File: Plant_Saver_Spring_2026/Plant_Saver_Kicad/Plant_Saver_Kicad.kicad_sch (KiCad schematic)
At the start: 21 parts, among them SW1 Up, SW2 Down, SW3 Change Screen, SW4 Select, SW5 Select, U14 CDBA140SL-HF, U18 ESP32-WROOM-32E-N16, U3 ESP32-WROOM-32D, U5 CDBA140SL-HF, U6 CDBA140SL-HF, U7 CDBA140SL-HF

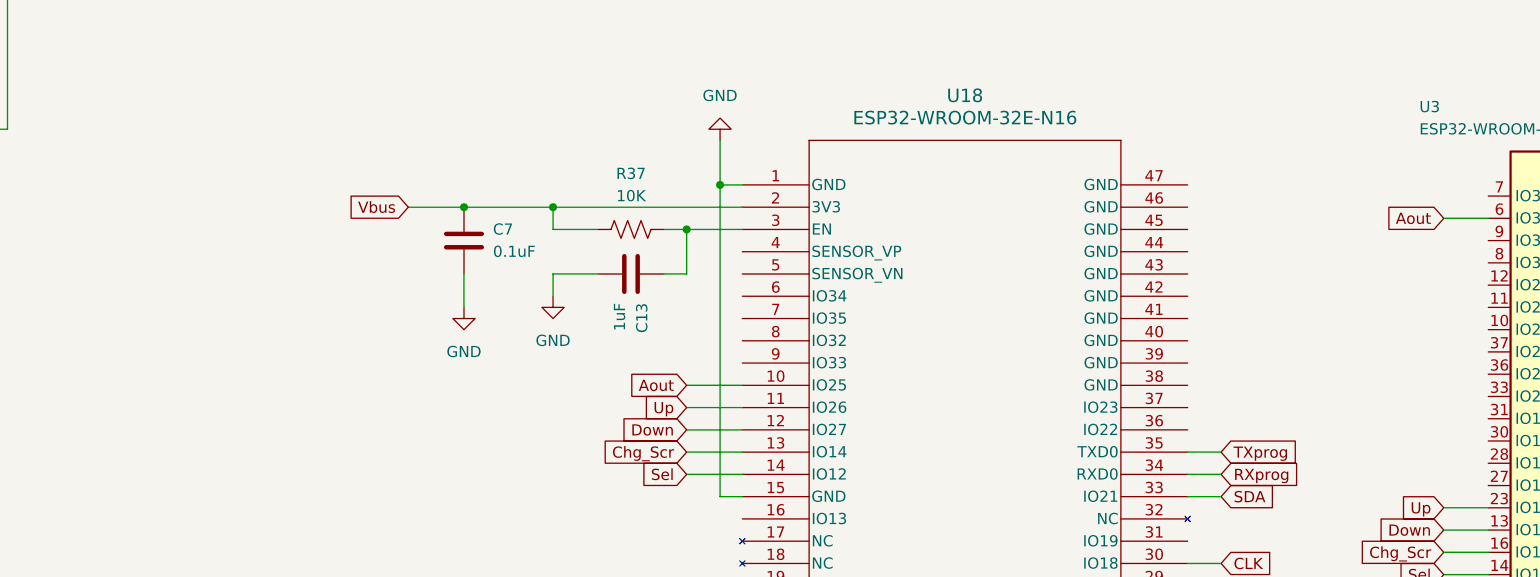
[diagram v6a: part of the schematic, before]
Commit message: Schematic updates
Added USB charge LEDs, updated PMOS gates, added micro connections and revised some of the charging set up.
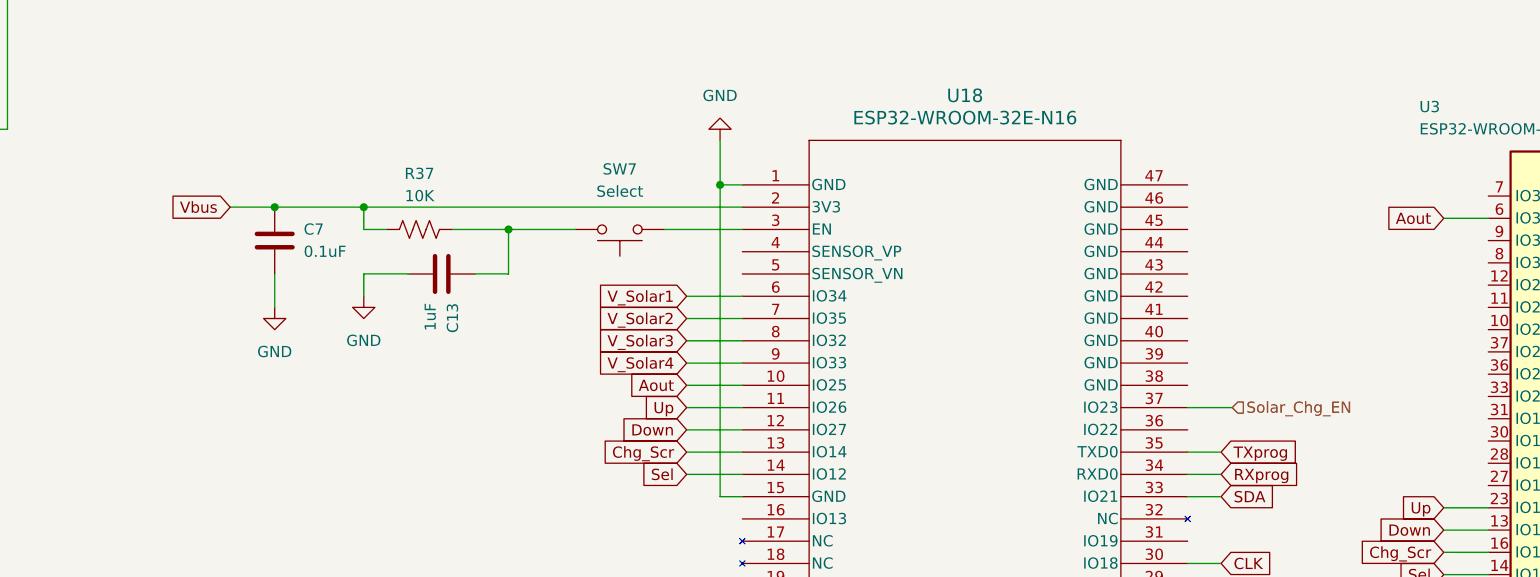
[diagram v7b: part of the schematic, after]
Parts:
- added SW7: Select, symbol Switch:SW_Push
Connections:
- net Solar_Chg_EN: now also U18.37 (IO23)
- net V_Solar1: now also U18.6 (IO34)
- net V_Solar2: now also U18.7 (IO35)
- net V_Solar3: now also U18.8 (IO32)
- net V_Solar4: now also U18.9 (IO33)
- net at C13.1, R37.2: now also SW7.2; no longer U18.3 (EN)
- new net: SW7.1, U18.3 (EN)
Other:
- moved on the sheet: C13, C7, R37

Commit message: Minor updates to charge/power
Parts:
- SC1, SC2, SC3, SC4: footprint (none) -> Capacitor_THT:C_Disc_D7.0mm_W2.5mm_P5.00mm
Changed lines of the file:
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@@
 			)
 		)
-		(property "Footprint" ""
+		(property "Footprint" "Capacitor_THT:C_Disc_D7.0mm_W2.5mm_P5.00mm"
 			(at 110.49 157.226 90)
 			(effects
@@
 			)
 		)
-		(property "Footprint" ""
+		(property "Footprint" "Capacitor_THT:C_Disc_D7.0mm_W2.5mm_P5.00mm"
 			(at 55.88 157.226 90)
 			(effects
@@
 			)
 		)
-		(property "Footprint" ""
+		(property "Footprint" "Capacitor_THT:C_Disc_D7.0mm_W2.5mm_P5.00mm"
 			(at 83.82 157.226 90)
 			(effects
@@
 			)
 		)
-		(property "Footprint" ""
+		(property "Footprint" "Capacitor_THT:C_Disc_D7.0mm_W2.5mm_P5.00mm"
 			(at 27.94 157.226 90)
 			(effects
